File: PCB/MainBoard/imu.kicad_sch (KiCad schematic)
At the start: 4 parts, among them IC1 ICM-42670-P

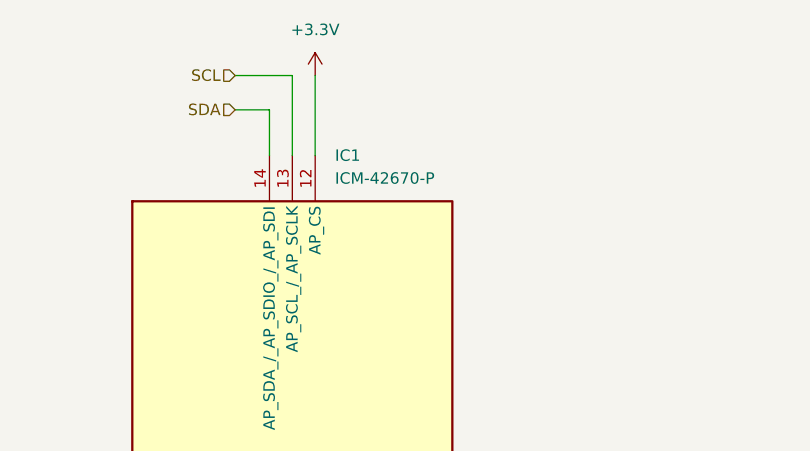
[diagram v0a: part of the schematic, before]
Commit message: Repaired IMU and ESP symbols and footprints
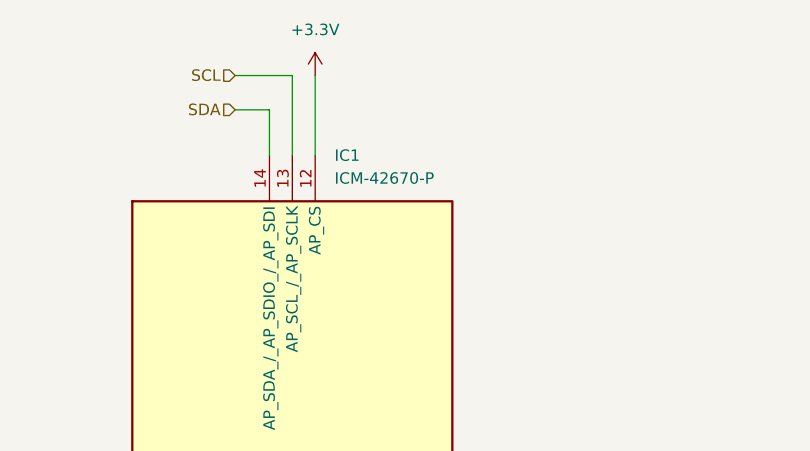
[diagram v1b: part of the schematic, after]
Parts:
- removed IC1: ICM-42670-P, PlajTime_Library:ICM42670P, symbol PlajTime:ICM-42670-P
- added IC1: ICM-42670-P, Components:ICM42670P, symbol Components:ICM-42670-P
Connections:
- net +3.3V: now also IC1.12 (AP_CS), IC1.5 (VDDIO), IC1.8 (VDD)
- net AP_AD0: now also IC1.1 (AP_SDO_/_AP_AD0)
- net GND: now also IC1.6 (GND), IC1.7 (FSYNC)
- net INT1: now also IC1.4 (INT1_/_INT)
- net INT2: now also IC1.9 (INT2)
- net SCL: now also IC1.13 (AP_SCL_/_AP_SCLK)
- net SDA: now also IC1.14 (AP_SDA_/_AP_SDIO_/_AP_SDI)
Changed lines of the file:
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@@
 (kicad_sch
-	(version 20231120)
+	(version 20250114)
 	(generator "eeschema")
-	(generator_version "8.0")
+	(generator_version "9.0")
 	(paper "A4")
 	(junction
@@
 		(shape input)
 		(at 92.71 45.72 180)
-		(fields_autoplaced yes)
 		(effects
 			(font
@@
 		(shape input)
 		(at 121.92 99.06 0)
-		(fields_autoplaced yes)
 		(effects
 			(font
@@
 		(shape input)
 		(at 66.04 101.6 180)
-		(fields_autoplaced yes)
 		(effects
 			(font
@@
 		(shape input)
 		(at 92.71 41.91 180)
-		(fields_autoplaced yes)
 		(effects
 			(font
@@
 		(shape input)
 		(at 66.04 93.98 180)
-		(fields_autoplaced yes)
 		(effects
 			(font
@@
 	)
 	(symbol
-		(lib_id "PlajTime:ICM-42670-P")
-		(at 76.2 93.98 0)
-		(unit 1)
-		(exclude_from_sim no)
-		(in_bom yes)
-		(on_board yes)
-		(dnp no)
-		(fields_autoplaced yes)
-		(property "Reference" "IC1"
-			(at 103.7941 50.8 0)
-			(effects
-				(font
-					(size 1.27 1.27)
-				)
-				(justify left)
-			)
-		)
-		(property "Value" "ICM-42670-P"
-			(at 103.7941 53.34 0)
-			(effects
-				(font
-					(size 1.27 1.27)
-				)
-				(justify left)
-			)
-		)
-		(property "Footprint" "PlajTime_Library:ICM42670P"
-			(at 118.11 153.34 0)
-			(effects
-				(font
-					(size 1.27 1.27)
-				)
-				(justify left top)
-				(hide yes)
-			)
-		)
-		(property "Datasheet" "https://3cfeqx1hf82y3xcoull08ihx-wpengine.netdna-ssl.com/wp-content/uploads/2021/07/DS-000451-ICM-42670-P-v1.0.pdf"
-			(at 118.11 253.34 0)
-			(effects
-				(font
-					(size 1.27 1.27)
-				)
-				(justify left top)
-				(hide yes)
-			)
-		)
-		(property "Description" "IMUs - Inertial Measurement Units Low-Power, Premium Performance 6-Axis MotionTrackingTM IMU with I3C, I2C and SPI interface in 2.5mm x 3mm Package"
-			(at 76.2 93.98 0)
-			(effects
-				(font
-					(size 1.27 1.27)
-				)
-				(hide yes)
-			)
-		)
-		(property "Height" ""
-			(at 118.11 453.34 0)
-			(effects
-				(font
-					(size 1.27 1.27)
-				)
-				(justify left top)
-				(hide yes)
-			)
-		)
-		(property "Mouser Part Number" "410-ICM-42670-P"
-			(at 118.11 553.34 0)
-			(effects
-				(font
-					(size 1.27 1.27)
-				)
-				(justify left top)
-				(hide yes)
-			)
-		)
-		(property "Mouser Price/Stock" "https://www.mouser.co.uk/ProductDetail/TDK-InvenSense/ICM-42670-P?qs=iLbezkQI%252BsgK8sMF5V7fQQ%3D%3D"
-			(at 118.11 653.34 0)
-			(effects
-				(font
-					(size 1.27 1.27)
-				)
-				(justify left top)
-				(hide yes)
-			)
-		)
-		(property "Manufacturer_Name" "TDK"
-			(at 118.11 753.34 0)
-			(effects
-				(font
-					(size 1.27 1.27)
-				)
-				(justify left top)
-				(hide yes)
-			)
-		)
-		(property "Manufacturer_Part_Number" "ICM-42670-P"
-			(at 118.11 853.34 0)
-			(effects
-				(font
-					(size 1.27 1.27)
-				)
-				(justify left top)
-				(hide yes)
-			)
-		)
-		(property "Description_1" ""
-			(at 76.2 93.98 0)
-			(effects
-				(font
-					(size 1.27 1.27)
-				)
-				(hide yes)
-			)
-		)
-		(pin "9"
-		)
-		(pin "5"
-		)
-		(pin "7"
-		)
-		(pin "8"
-		)
-		(pin "12"
-		)
-		(pin "2"
-		)
-		(pin "13"
-		)
-		(pin "14"
-		)
-		(pin "3"
-		)
-		(pin "11"
-		)
-		(pin "10"
-		)
-		(pin "1"
-		)
-		(pin "6"
-		)
-		(pin "4"
-		)
-		(instances
-			(project "MainBoard"
-				(path "/4b463b93-bd96-4cf6-bfe2-9d8869b16347/080fd4b0-d484-4a9f-b530-51ac3d24ee6a"
-					(reference "IC1")
-					(unit 1)
-				)
-			)
-		)
-	)
-	(symbol
 		(lib_id "power:+3.3V")
 		(at 83.82 132.08 90)
@@
 					(unit 1)
 				)
+			)
+		)
+	)
+	(symbol
+		(lib_id "Components:ICM-42670-P")
+		(at 76.2 93.98 0)
+		(unit 1)
+		(exclude_from_sim no)
+		(in_bom yes)
+		(on_board yes)
+		(dnp no)
+		(fields_autoplaced yes)
+		(property "Reference" "IC1"
+			(at 103.7433 50.8 0)
+			(effects
+				(font
+					(size 1.27 1.27)
+				)
+				(justify left)
+			)
+		)
+		(property "Value" "ICM-42670-P"
+			(at 103.7433 53.34 0)
+			(effects
+				(font
+					(size 1.27 1.27)
+				)
+				(justify left)
+			)
+		)
+		(property "Footprint" "Components:ICM42670P"
+			(at 118.11 153.34 0)
+			(effects
+				(font
+					(size 1.27 1.27)
+				)
+				(justify left top)
+				(hide yes)
+			)
+		)
+		(property "Datasheet" "https://3cfeqx1hf82y3xcoull08ihx-wpengine.netdna-ssl.com/wp-content/uploads/2021/07/DS-000451-ICM-42670-P-v1.0.pdf"
+			(at 118.11 253.34 0)
+			(effects
+				(font
+					(size 1.27 1.27)
+				)
+				(justify left top)
+				(hide yes)
+			)
+		)
+		(property "Description" "IMUs - Inertial Measurement Units Low-Power, Premium Performance 6-Axis MotionTrackingTM IMU with I3C, I2C and SPI interface in 2.5mm x 3mm Package"
+			(at 76.2 93.98 0)
+			(effects
+				(font
+					(size 1.27 1.27)
+				)
+				(hide yes)
+			)
+		)
+		(property "Height" ""
+			(at 118.11 453.34 0)
+			(effects
+				(font
+					(size 1.27 1.27)
+				)
+				(justify left top)
+				(hide yes)
+			)
+		)
+		(property "Mouser Part Number" "410-ICM-42670-P"
+			(at 118.11 553.34 0)
+			(effects
+				(font
+					(size 1.27 1.27)
+				)
+				(justify left top)
+				(hide yes)
+			)
+		)
+		(property "Mouser Price/Stock" "https://www.mouser.co.uk/ProductDetail/TDK-InvenSense/ICM-42670-P?qs=iLbezkQI%252BsgK8sMF5V7fQQ%3D%3D"
+			(at 118.11 653.34 0)
+			(effects
+				(font
+					(size 1.27 1.27)
+				)
+				(justify left top)
+				(hide yes)
+			)
+		)
+		(property "Manufacturer_Name" "TDK"
+			(at 118.11 753.34 0)
+			(effects
+				(font
+					(size 1.27 1.27)
+				)
+				(justify left top)
+				(hide yes)
+			)
+		)
+		(property "Manufacturer_Part_Number" "ICM-42670-P"
+			(at 118.11 853.34 0)
+			(effects
+				(font
+					(size 1.27 1.27)
+				)
+				(justify left top)
+				(hide yes)
+			)
+		)
+		(pin "1"
+		)
+		(pin "11"
+		)
+		(pin "10"
+		)
+		(pin "6"
+		)
+		(pin "5"
+		)
+		(pin "13"
+		)
+		(pin "2"
+		)
+		(pin "14"
+		)
+		(pin "7"
+		)
+		(pin "9"
+		)
+		(pin "4"
+		)
+		(pin "8"
+		)
+		(pin "12"
+		)
+		(pin "3"
+		)
+		(instances
+			(project ""
+				(path "/4b463b93-bd96-4cf6-bfe2-9d8869b16347/080fd4b0-d484-4a9f-b530-51ac3d24ee6a"
+					(reference "IC1")
+					(unit 1)
+				)

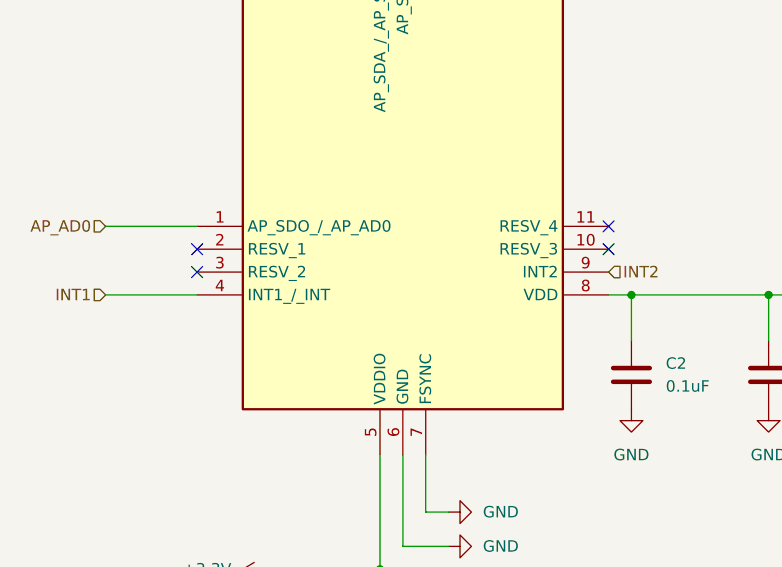
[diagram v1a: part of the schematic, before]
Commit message: Added Buck converter
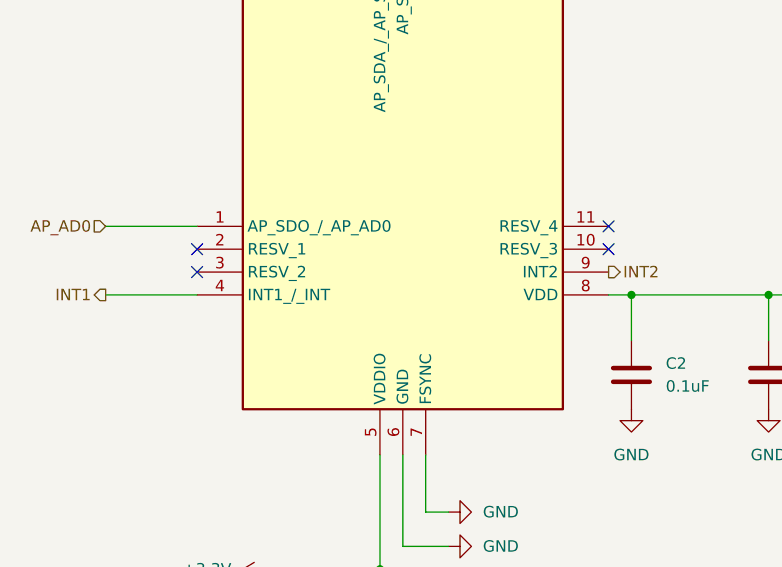
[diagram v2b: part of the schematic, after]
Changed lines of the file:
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@@
 	)
 	(hierarchical_label "INT2"
-		(shape input)
+		(shape output)
 		(at 121.92 99.06 0)
 		(effects
@@
 	)
 	(hierarchical_label "INT1"
-		(shape input)
+		(shape output)
 		(at 66.04 101.6 180)
 		(effects
